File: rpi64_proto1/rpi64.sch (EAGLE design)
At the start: 67 parts, among them Q1 BSS123, Q2 BSS123

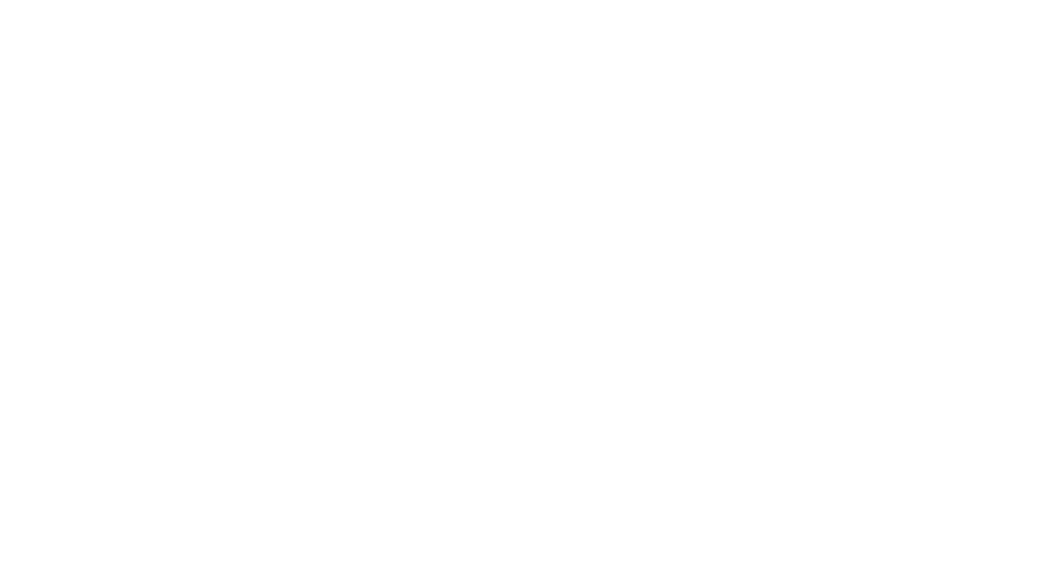
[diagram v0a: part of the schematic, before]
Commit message: Added front connectors
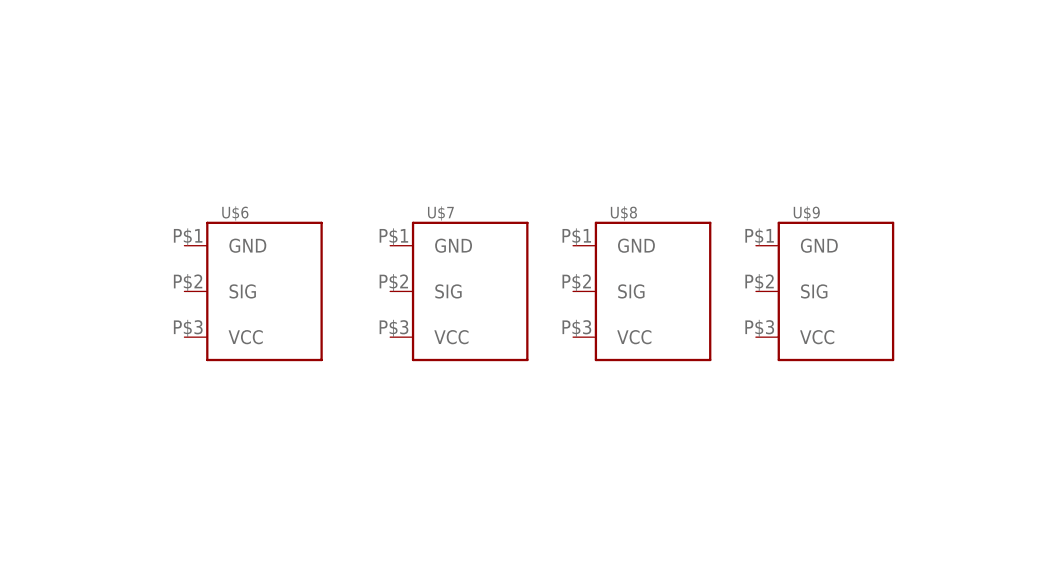
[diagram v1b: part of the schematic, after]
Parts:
- added U$6, U$7, U$8, U$9: N64_CONTROLER, rpi64:N64_CONTROLER
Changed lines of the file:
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@@
 <part name="R52" library="rcl" deviceset="R-EU_" device="R0603" value="1k"/>
 <part name="+3V10" library="supply1" deviceset="+3V3" device=""/>
+<part name="U$6" library="rpi64" deviceset="N64_CONTROLER" device=""/>
+<part name="U$7" library="rpi64" deviceset="N64_CONTROLER" device=""/>
+<part name="U$8" library="rpi64" deviceset="N64_CONTROLER" device=""/>
+<part name="U$9" library="rpi64" deviceset="N64_CONTROLER" device=""/>
 </parts>
 <sheets>
@@
 <instance part="R52" gate="G$1" x="299.72" y="91.44"/>
 <instance part="+3V10" gate="G$1" x="289.56" y="91.44" rot="R90"/>
+<instance part="U$6" gate="G$1" x="53.34" y="203.2"/>
+<instance part="U$7" gate="G$1" x="76.2" y="203.2"/>
+<instance part="U$8" gate="G$1" x="96.52" y="203.2"/>
+<instance part="U$9" gate="G$1" x="116.84" y="203.2"/>
 </instances>
 <busses>

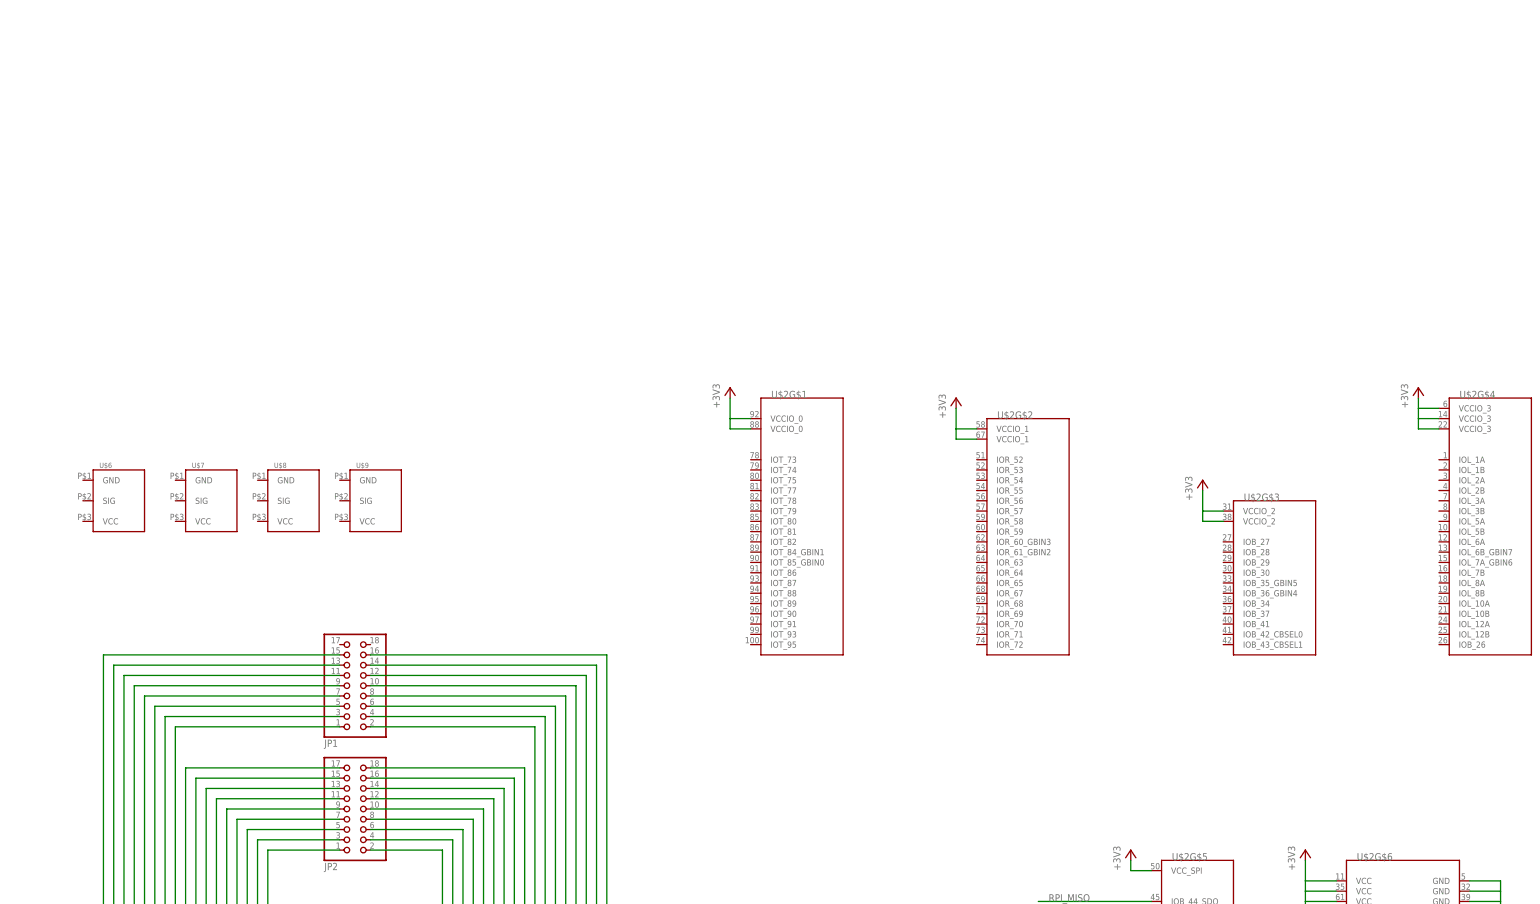
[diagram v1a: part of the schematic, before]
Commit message: Top layer of resistor placed
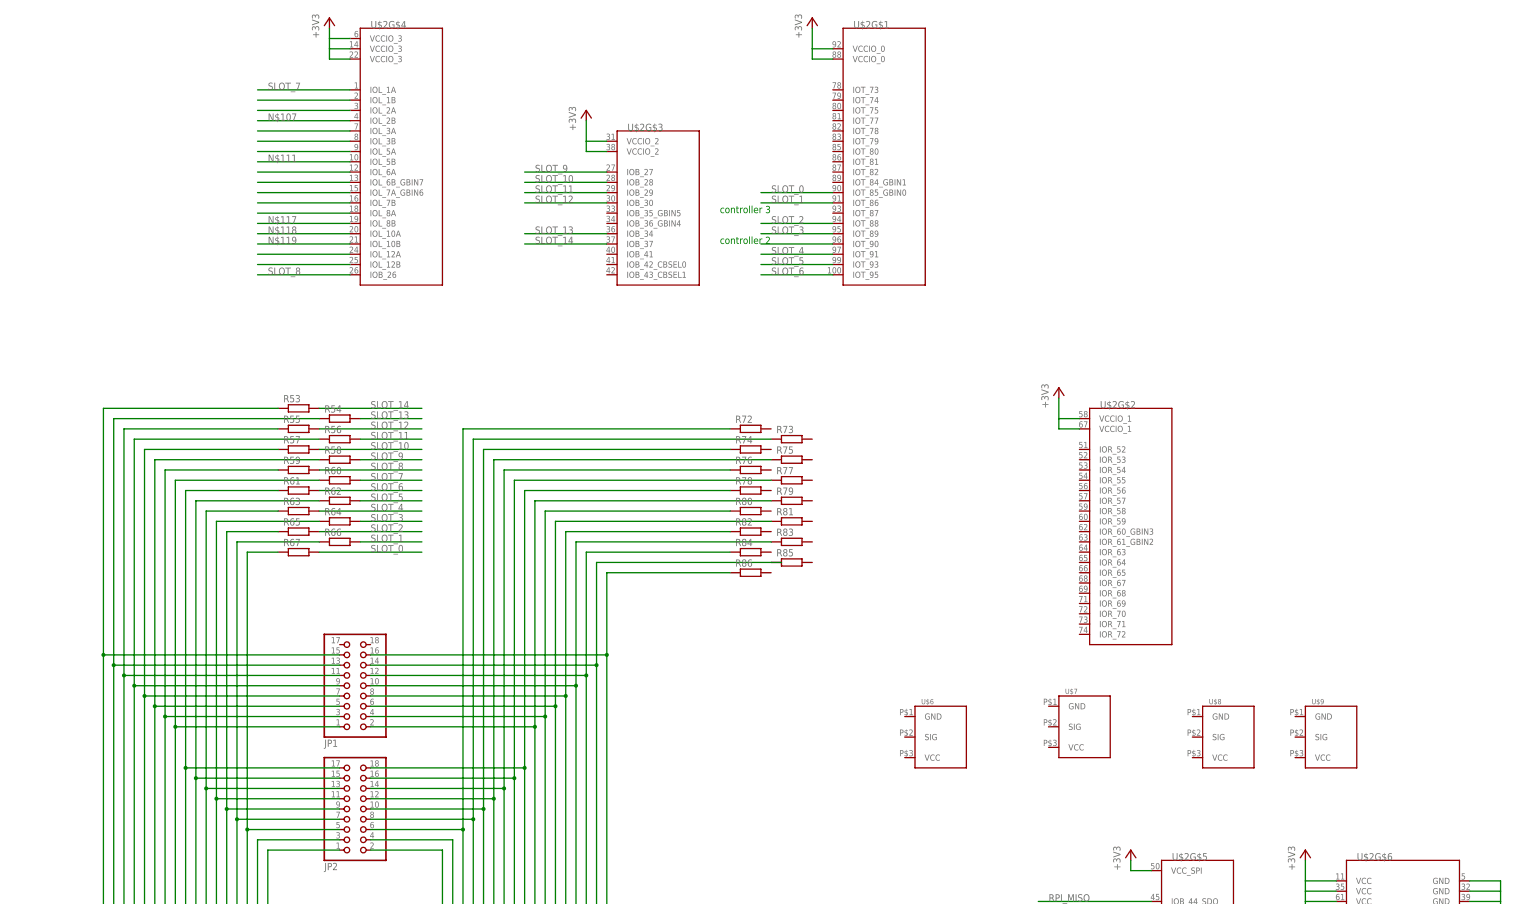
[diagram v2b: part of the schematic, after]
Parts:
- added R53, R54, R55, R56, R57, R58, R59, R60, R61, R62, R63, R64, R65, R66, R67, R72, R73, R74, R75, R76, R77, R78, R79, R80, R81, R82, R83, R84, R85, R86: (no value), rcl:R-EU_R0603
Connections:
- new net N$104: U$2G$4.IOL_12A
- new net N$105: JP1.14, R35.2, R85.1, U$1.P$35
- new net N$107: U$2G$4.IOL_2B
- new net N$109: U$2G$4.IOL_8A
- new net N$110: U$2G$1.IOT_90
- new net N$111: U$2G$4.IOL_5B
- new net N$112: U$2G$4.IOL_7B
- new net N$113: U$2G$4.IOL_7A_GBIN6
- new net N$114: U$2G$4.IOL_6B_GBIN7
- new net N$115: U$2G$4.IOL_6A
- new net N$116: U$2G$4.IOL_5A
- new net N$117: U$2G$4.IOL_8B
- new net N$118: U$2G$4.IOL_10A
- new net N$119: U$2G$4.IOL_10B
- new net N$120: U$2G$4.IOL_3B
- new net N$121: U$2G$4.IOL_3A
- new net N$122: U$2G$4.IOL_2A
- new net N$123: U$2G$4.IOL_1B
- new net SLOT_0: R67.2, U$2G$1.IOT_85_GBIN0
- new net SLOT_1: R66.2, U$2G$1.IOT_86
- new net SLOT_10: R57.2, U$2G$3.IOB_28
- new net SLOT_11: R56.2, U$2G$3.IOB_29
- new net SLOT_12: R55.2, U$2G$3.IOB_30
- new net SLOT_13: R54.2, U$2G$3.IOB_34
- new net SLOT_14: R53.2, U$2G$3.IOB_37
- new net SLOT_2: R65.2, U$2G$1.IOT_88
- new net SLOT_3: R64.2, U$2G$1.IOT_89
- new net SLOT_4: R63.2, U$2G$1.IOT_91
- new net SLOT_5: R62.2, U$2G$1.IOT_93
- new net SLOT_6: R61.2, U$2G$1.IOT_95
- new net SLOT_7: R60.2, U$2G$4.IOL_1A
- new net SLOT_8: R59.2, U$2G$4.IOB_26
- new net SLOT_9: R58.2, U$2G$3.IOB_27
- net N$53: now also R67.1
- net N$54: now also R66.1
- net N$55: now also R65.1
- net N$56: now also R64.1
- net N$57: now also R63.1
- net N$58: now also R62.1
- net N$59: now also R61.1
- net N$60: now also R60.1
- net N$61: now also R59.1
- net N$62: now also R58.1
- net N$63: now also R57.1
- net N$64: now also R56.1
- net N$65: now also R55.1
- net N$66: now also R54.1
- net N$67: now also R53.1
- net N$78: now also R72.1
- net N$79: now also R73.1
- net N$80: now also R74.1
- net N$81: now also R75.1
- net N$82: now also R76.1
- net N$83: now also R77.1
- net N$84: now also R78.1
- net N$85: now also R79.1
- net N$86: now also R80.1
- net N$87: now also R81.1
- net N$88: now also R82.1
- net N$89: now also R83.1
- net N$90: now also R84.1
- net N$91: now also U$2G$4.IOL_12B; no longer JP1.14, R35.2, U$1.P$35
- net N$92: now also R86.1
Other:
- note added: "controller 2"
- note added: "controller 3"
- moved on the sheet: U$2G$1, U$2G$2, U$2G$3, U$2G$4, U$6, U$7, U$8, U$9

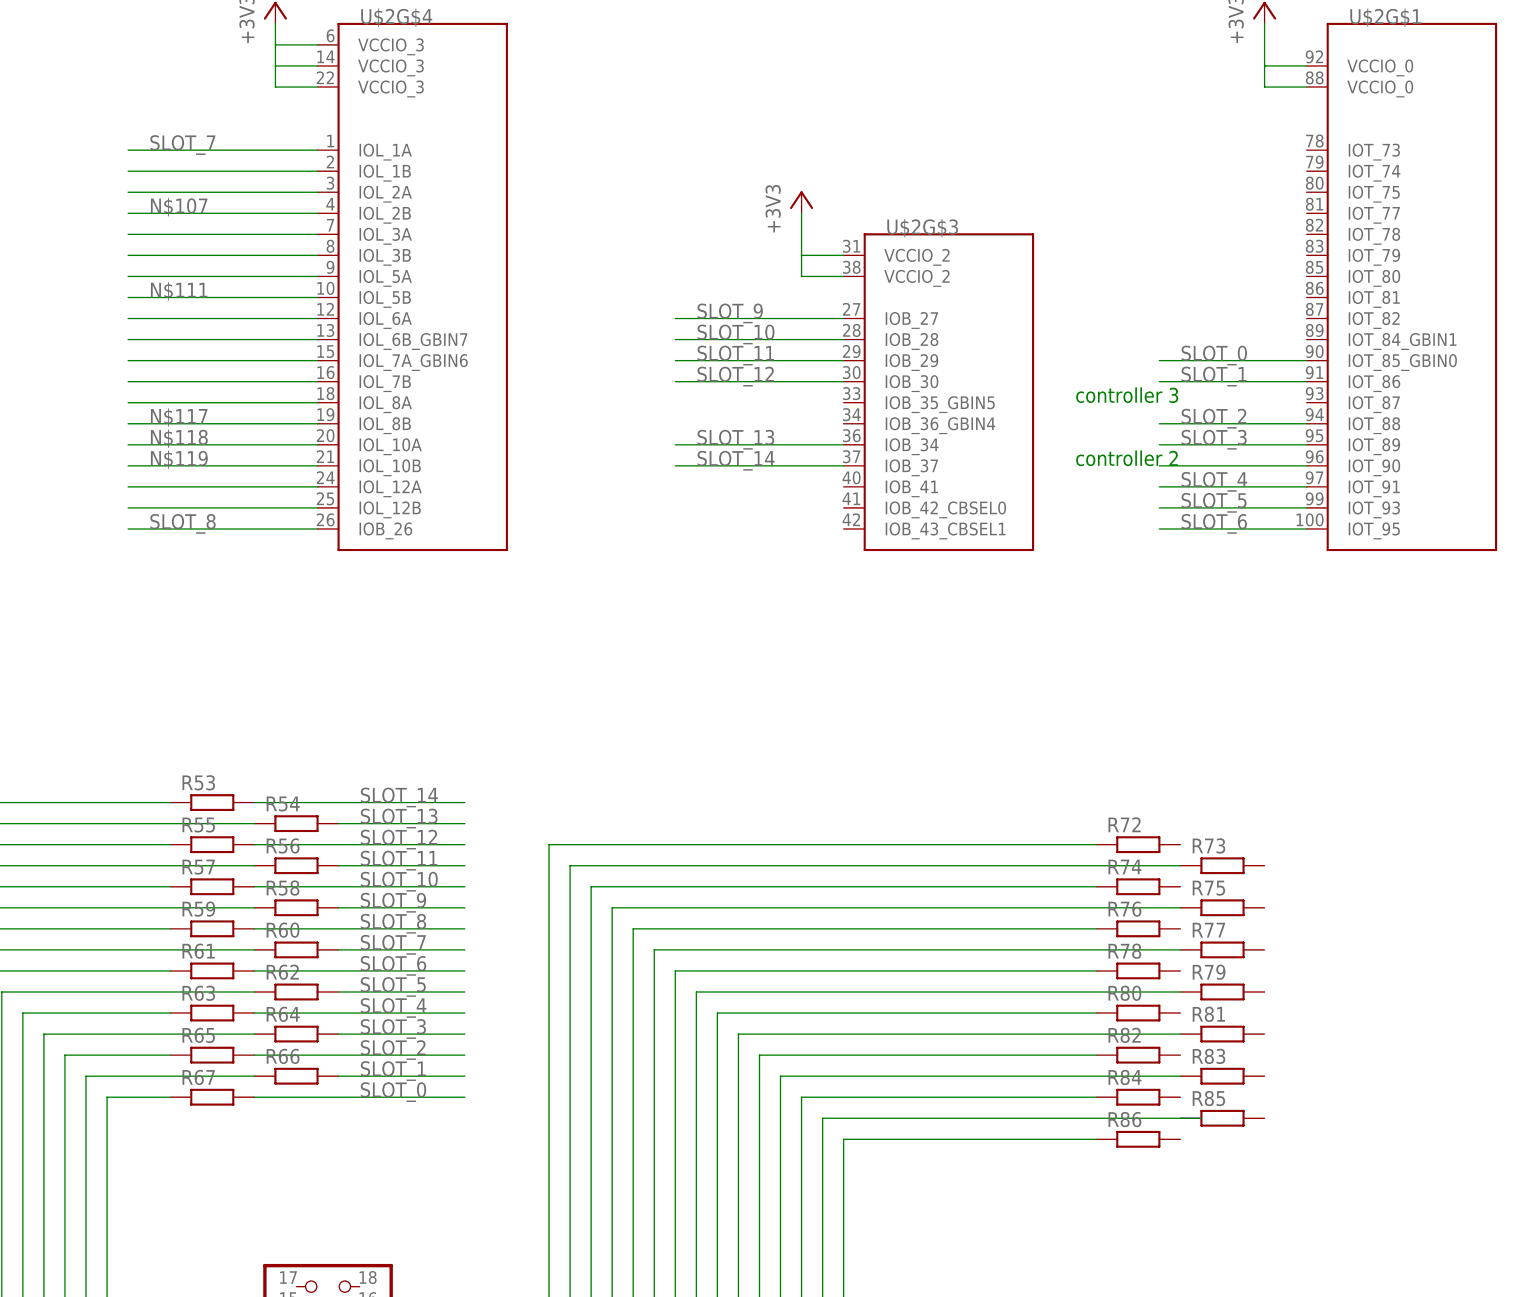
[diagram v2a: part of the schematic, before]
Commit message: Placed and routed all resistor for N64 slot
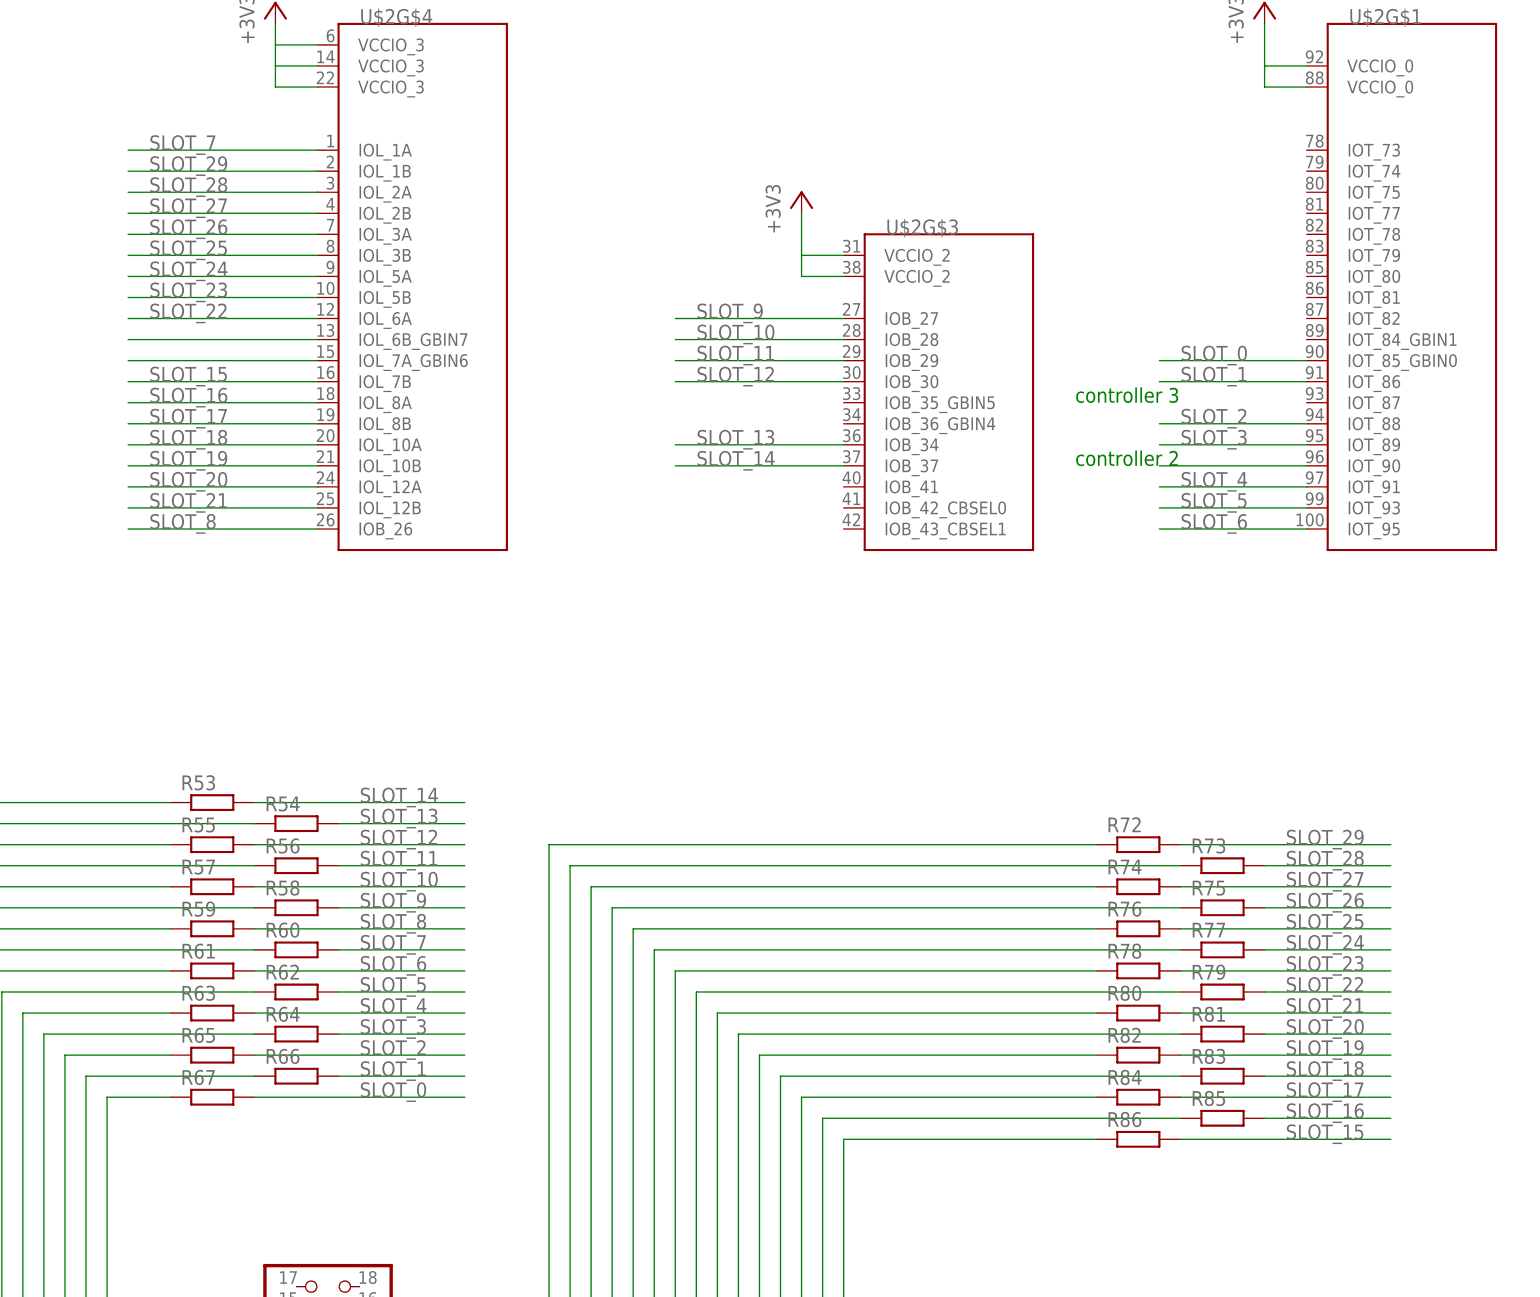
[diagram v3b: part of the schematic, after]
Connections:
- removed net N$104: U$2G$4.IOL_12A
- removed net N$107: U$2G$4.IOL_2B
- removed net N$109: U$2G$4.IOL_8A
- removed net N$111: U$2G$4.IOL_5B
- removed net N$112: U$2G$4.IOL_7B
- removed net N$115: U$2G$4.IOL_6A
- removed net N$116: U$2G$4.IOL_5A
- removed net N$117: U$2G$4.IOL_8B
- removed net N$118: U$2G$4.IOL_10A
- removed net N$119: U$2G$4.IOL_10B
- removed net N$120: U$2G$4.IOL_3B
- removed net N$121: U$2G$4.IOL_3A
- removed net N$122: U$2G$4.IOL_2A
- removed net N$123: U$2G$4.IOL_1B
- removed net N$91: U$2G$4.IOL_12B
- new net SLOT_15: R86.2, U$2G$4.IOL_7B
- new net SLOT_16: R85.2, U$2G$4.IOL_8A
- new net SLOT_17: R84.2, U$2G$4.IOL_8B
- new net SLOT_18: R83.2, U$2G$4.IOL_10A
- new net SLOT_19: R82.2, U$2G$4.IOL_10B
- new net SLOT_20: R81.2, U$2G$4.IOL_12A
- new net SLOT_21: R80.2, U$2G$4.IOL_12B
- new net SLOT_22: R79.2, U$2G$4.IOL_6A
- new net SLOT_23: R78.2, U$2G$4.IOL_5B
- new net SLOT_24: R77.2, U$2G$4.IOL_5A
- new net SLOT_25: R76.2, U$2G$4.IOL_3B
- new net SLOT_26: R75.2, U$2G$4.IOL_3A
- new net SLOT_27: R74.2, U$2G$4.IOL_2B
- new net SLOT_28: R73.2, U$2G$4.IOL_2A
- new net SLOT_29: R72.2, U$2G$4.IOL_1B
